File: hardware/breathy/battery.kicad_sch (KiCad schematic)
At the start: 7 parts, among them J3 Screw_Terminal_01x02, Q3 PMV37ENEAR, Q4 PMV37ENEAR, U5 DW01A

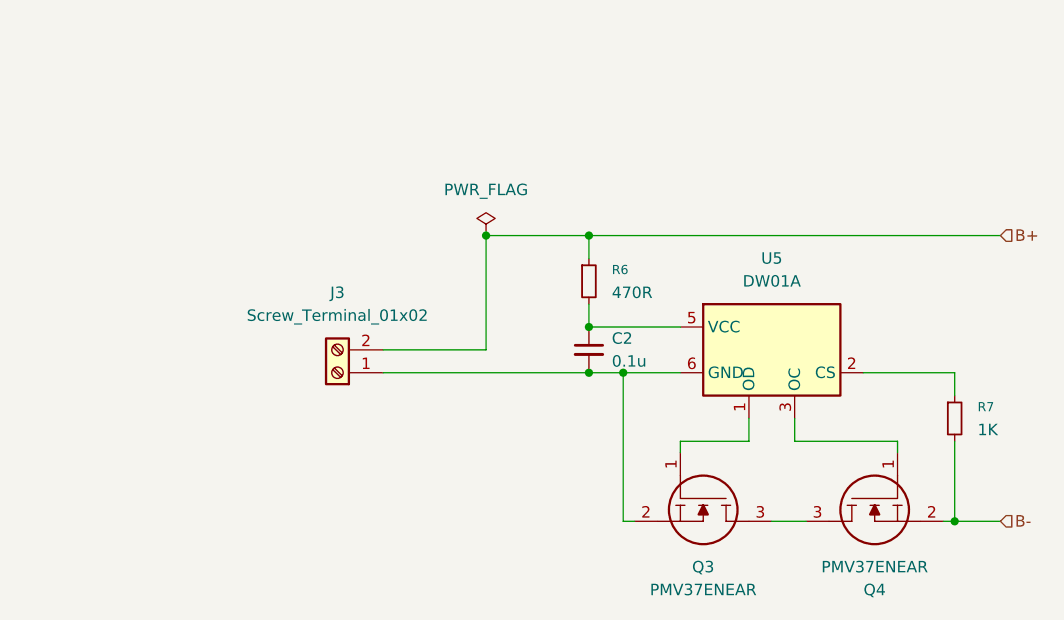
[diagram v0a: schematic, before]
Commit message: test points, headers, indicators, no battery sim
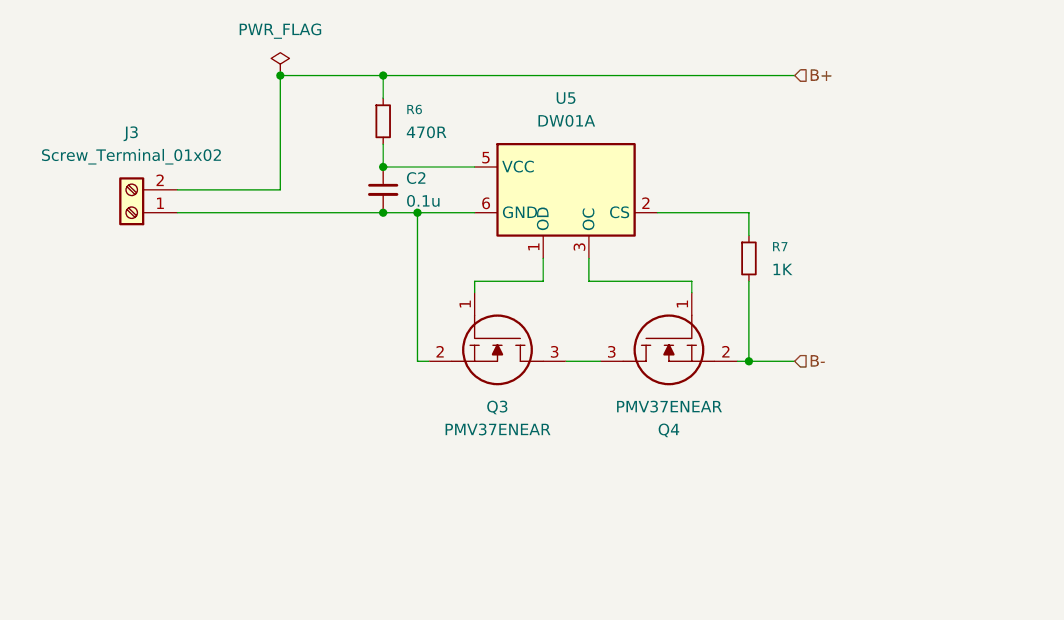
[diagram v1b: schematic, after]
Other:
- moved on the sheet: C2, J3, Q3, Q4, R6, R7, U5

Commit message: adding pdf schematics
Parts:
- C14: renamed from C2; footprint (none) -> Capacitor_SMD:C_0805_2012Metric
- J6: renamed from J3; footprint (none) -> TerminalBlock:TerminalBlock_MaiXu_MX126-5.0-02P_1x02_P5.00mm
- R29: renamed from R6; footprint Resistor_SMD:R_1206_3216Metric_Pad1.30x1.75mm_HandSolder -> Resistor_SMD:R_0805_2012Metric
- R30: renamed from R7; footprint Resistor_SMD:R_1206_3216Metric_Pad1.30x1.75mm_HandSolder -> Resistor_SMD:R_1206_3216Metric
- renumbered Q3 to Q7, Q4 to Q8, U5 to U9
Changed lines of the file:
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@@
 		(dnp no)
 		(fields_autoplaced yes)
-		(property "Reference" "J3"
+		(property "Reference" "J6"
 			(at 26.67 33.02 0)
 			(show_name no)
@@
 			)
 		)
-		(property "Footprint" ""
+		(property "Footprint" "TerminalBlock:TerminalBlock_MaiXu_MX126-5.0-02P_1x02_P5.00mm"
 			(at 26.67 41.91 0)
 			(hide yes)
@@
 			(project "breathy"
 				(path "/b1c49805-8a08-4cdd-9984-c6cc27843db8/7679b0b1-00f0-47a2-a61b-179ee4aaeb30"
-					(reference "J3")
+					(reference "J6")
 					(unit 1)
 				)
@@
 		(in_pos_files yes)
 		(dnp no)
-		(property "Reference" "Q4"
+		(property "Reference" "Q8"
 			(at 86.36 66.04 90)
 			(show_name no)
@@
 			(project "breathy"
 				(path "/b1c49805-8a08-4cdd-9984-c6cc27843db8/7679b0b1-00f0-47a2-a61b-179ee4aaeb30"
-					(reference "Q4")
+					(reference "Q8")
 					(unit 1)
 				)
@@
 		(dnp no)
 		(fields_autoplaced yes)
-		(property "Reference" "R6"
+		(property "Reference" "R29"
 			(at 57.15 30.4799 0)
 			(show_name no)
@@
 			)
 		)
-		(property "Footprint" "Resistor_SMD:R_1206_3216Metric_Pad1.30x1.75mm_HandSolder"
+		(property "Footprint" "Resistor_SMD:R_0805_2012Metric"
 			(at 54.61 31.75 0)
 			(hide yes)
@@
 			(project "breathy"
 				(path "/b1c49805-8a08-4cdd-9984-c6cc27843db8/7679b0b1-00f0-47a2-a61b-179ee4aaeb30"
-					(reference "R6")
+					(reference "R29")
 					(unit 1)
 				)
@@
 		(dnp no)
 		(fields_autoplaced yes)
-		(property "Reference" "U5"
+		(property "Reference" "U9"
 			(at 74.93 29.21 0)
 			(show_name no)
@@
 			(project "breathy"
 				(path "/b1c49805-8a08-4cdd-9984-c6cc27843db8/7679b0b1-00f0-47a2-a61b-179ee4aaeb30"
-					(reference "U5")
+					(reference "U9")
 					(unit 1)
 				)
@@
 		(dnp no)
 		(fields_autoplaced yes)
-		(property "Reference" "Q3"
+		(property "Reference" "Q7"
 			(at 67.31 63.5 90)
 			(show_name no)
@@
 			(project "breathy"
 				(path "/b1c49805-8a08-4cdd-9984-c6cc27843db8/7679b0b1-00f0-47a2-a61b-179ee4aaeb30"
-					(reference "Q3")
+					(reference "Q7")
 					(unit 1)
 				)
@@
 		(dnp no)
 		(fields_autoplaced yes)
-		(property "Reference" "C2"
+		(property "Reference" "C14"
 			(at 57.15 38.1062 0)
 			(show_name no)
@@
 			)
 		)
-		(property "Footprint" ""
+		(property "Footprint" "Capacitor_SMD:C_0805_2012Metric"
 			(at 54.61 39.37 0)
 			(hide yes)
@@
 			(project "breathy"
 				(path "/b1c49805-8a08-4cdd-9984-c6cc27843db8/7679b0b1-00f0-47a2-a61b-179ee4aaeb30"
-					(reference "C2")
+					(reference "C14")
 					(unit 1)
 				)
@@
 		(dnp no)
 		(fields_autoplaced yes)
-		(property "Reference" "R7"
+		(property "Reference" "R30"
 			(at 97.79 45.7199 0)
 			(show_name no)
@@
 			)
 		)
-		(property "Footprint" "Resistor_SMD:R_1206_3216Metric_Pad1.30x1.75mm_HandSolder"
+		(property "Footprint" "Resistor_SMD:R_1206_3216Metric"
 			(at 95.25 46.99 0)
 			(hide yes)
@@
 			(project "breathy"
 				(path "/b1c49805-8a08-4cdd-9984-c6cc27843db8/7679b0b1-00f0-47a2-a61b-179ee4aaeb30"
-					(reference "R7")
+					(reference "R30")
 					(unit 1)
 				)
@@
 		(dnp no)
 		(fields_autoplaced yes)
-		(property "Reference" "#FLG01"
+		(property "Reference" "#FLG02"
 			(at 43.18 24.765 0)
 			(hide yes)
@@
 			(project "breathy"
 				(path "/b1c49805-8a08-4cdd-9984-c6cc27843db8/7679b0b1-00f0-47a2-a61b-179ee4aaeb30"
-					(reference "#FLG01")
+					(reference "#FLG02")
 					(unit 1)
 				)
